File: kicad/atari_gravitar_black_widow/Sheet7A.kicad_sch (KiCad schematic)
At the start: 28 parts

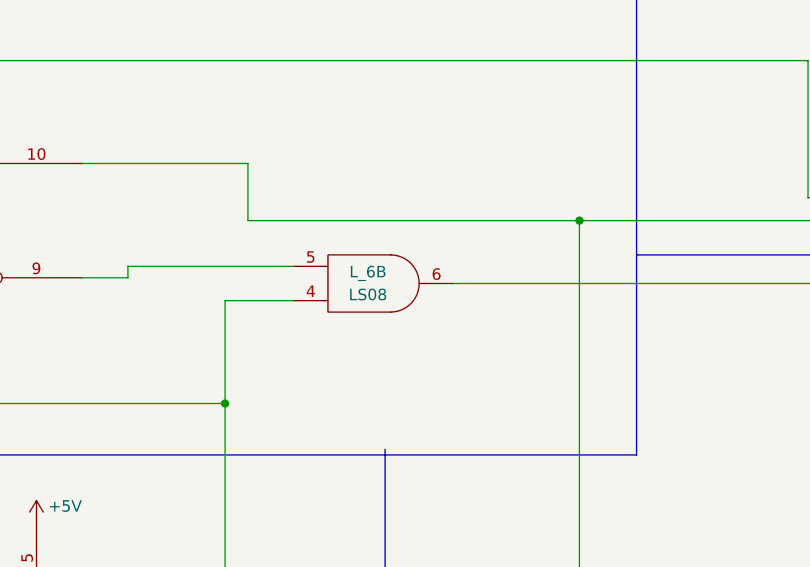
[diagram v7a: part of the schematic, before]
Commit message: more ttl placements
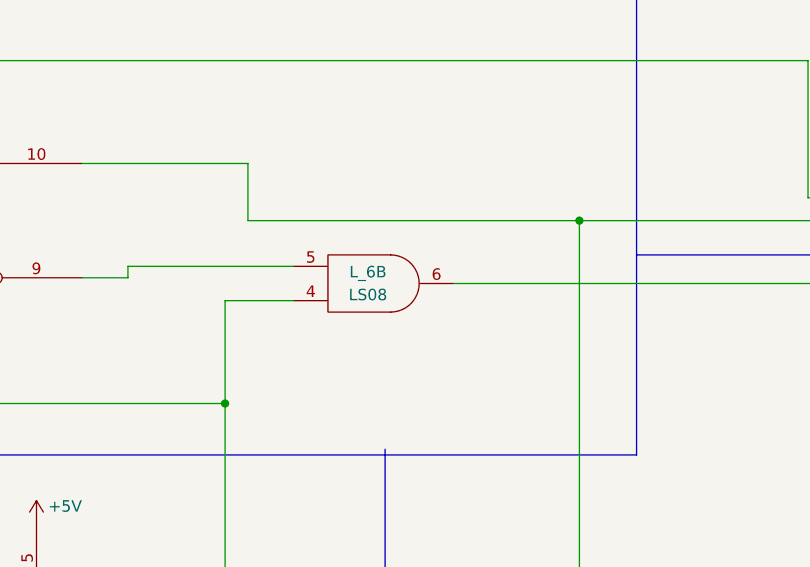
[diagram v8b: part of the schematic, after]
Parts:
- C_7, D_7, E_5: footprint (none) -> Star_Wars_Vector_PCB:DIP16
- E_3, F_3, F_5, H_3, H_5: footprint (none) -> Star_Wars_Vector_PCB:DIP14
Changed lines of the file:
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@@
     (property "Reference" "E_5" (id 0) (at 224.79 111.125 0))
     (property "Value" "LS109A" (id 1) (at 224.79 114.935 0))
-    (property "Footprint" "" (id 2) (at 224.79 114.935 0)
+    (property "Footprint" "Star_Wars_Vector_PCB:DIP16" (id 2) (at 224.79 114.935 0)
       (effects (font (size 1.27 1.27)) hide)
     )
@@
       (effects (font (size 1.27 1.27)) (justify left))
     )
-    (property "Footprint" "" (id 2) (at 238.76 166.37 0)
+    (property "Footprint" "Star_Wars_Vector_PCB:DIP16" (id 2) (at 238.76 166.37 0)
       (effects (font (size 1.27 1.27)) hide)
     )
@@
     (property "Reference" "D_7" (id 0) (at 54.61 300.355 0))
     (property "Value" "LS175" (id 1) (at 55.245 304.165 0))
-    (property "Footprint" "" (id 2) (at 55.88 302.895 0)
+    (property "Footprint" "Star_Wars_Vector_PCB:DIP16" (id 2) (at 55.88 302.895 0)
       (effects (font (size 1.27 1.27)) hide)
     )
@@
     (property "Reference" "C_7" (id 0) (at 116.84 298.45 0))
     (property "Value" "LS191" (id 1) (at 116.84 302.26 0))
-    (property "Footprint" "" (id 2) (at 117.475 299.085 0)
+    (property "Footprint" "Star_Wars_Vector_PCB:DIP16" (id 2) (at 117.475 299.085 0)
       (effects (font (size 1.27 1.27)) hide)
     )
@@
       (effects (font (size 1.27 1.27)) (justify left))
     )
-    (property "Footprint" "" (id 2) (at 114.935 264.795 0)
+    (property "Footprint" "Star_Wars_Vector_PCB:DIP14" (id 2) (at 114.935 264.795 0)
       (effects (font (size 1.27 1.27)) hide)
     )
@@
     (property "Reference" "F_5" (id 0) (at 422.275 290.83 0))
     (property "Value" "LS11" (id 1) (at 422.275 292.735 0))
-    (property "Footprint" "" (id 2) (at 422.275 291.465 0)
+    (property "Footprint" "Star_Wars_Vector_PCB:DIP14" (id 2) (at 422.275 291.465 0)
       (effects (font (size 1.27 1.27)) hide)
     )
@@
     (property "Reference" "E_3" (id 0) (at 298.45 330.835 0))
     (property "Value" "LS00" (id 1) (at 298.45 333.375 0))
-    (property "Footprint" "" (id 2) (at 298.45 332.74 0)
+    (property "Footprint" "Star_Wars_Vector_PCB:DIP14" (id 2) (at 298.45 332.74 0)
       (effects (font (size 1.27 1.27)) hide)
     )
@@
       (effects (font (size 1.27 1.27)) (justify left))
     )
-    (property "Footprint" "" (id 2) (at 499.745 271.145 0)
+    (property "Footprint" "Star_Wars_Vector_PCB:DIP14" (id 2) (at 499.745 271.145 0)
       (effects (font (size 1.27 1.27)) hide)
     )
@@
       (effects (font (size 1.27 1.27)) (justify left))
     )
-    (property "Footprint" "" (id 2) (at 546.735 262.89 0)
-      (effects (font (size 1.27 1.27)) hide)
-    )
+    (property "Footprint" "Star_Wars_Vector_PCB:DIP14" (id 2) (at 546.735 262.89 0)
+      (effects (font (size 1.27 1.27)) hide)
+    )
